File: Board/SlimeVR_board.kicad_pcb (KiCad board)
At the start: 2 copper layers, 61 x 50 mm, 46 parts, among them IC1 HT7833, J1 USB_C_Receptacle_USB2.0_16P, J2 JST-PH, J3 SMD_Pads, J4 SMD_Pads, J5 Conn_01x01_Pin, J6 Conn_01x01_Pin, J7 JTX-HX-A-1, J8 JTX-HX-A-1, Q1 DMP3099L-7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

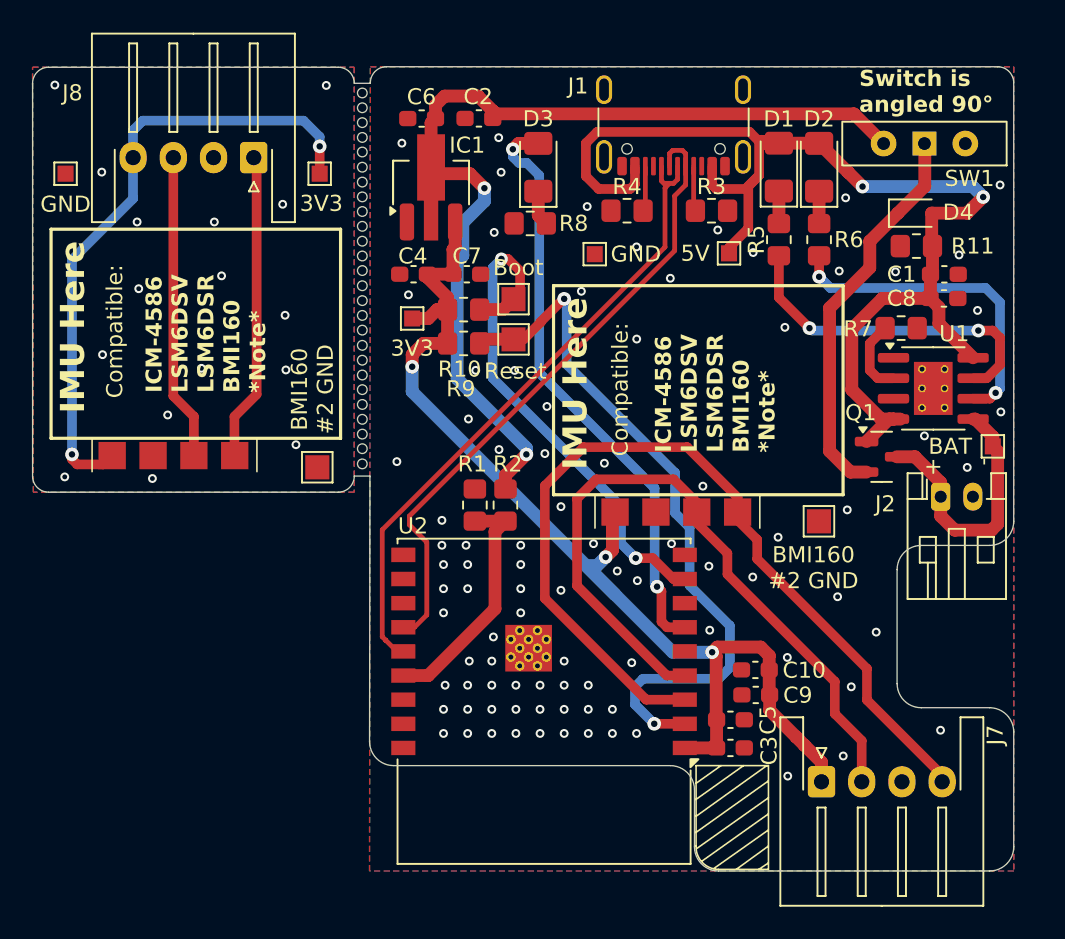
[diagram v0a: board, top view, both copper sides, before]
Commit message: Nweset Board update
Update log:
- Moved 3.3 conventor closer to esp for more stability
- Properly labeled Boot and Reset pads with own GND
- New and remade grafic
- Two capacitators no more needed (material saving :D)
- New Logo (I got some logo of my probebly will change idk)
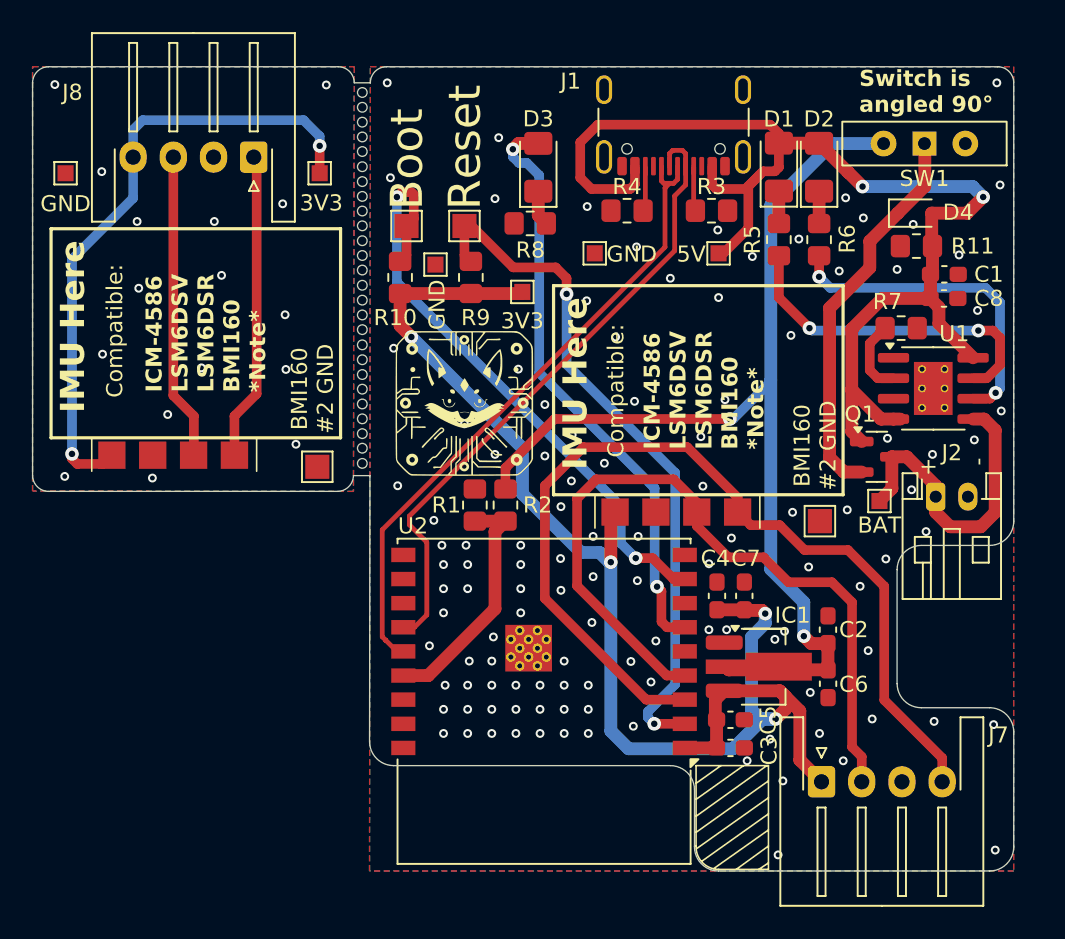
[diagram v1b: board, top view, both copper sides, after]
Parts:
- removed C10: 100nF, Capacitor_SMD:C_0603_1608Metric_Pad1.08x0.95mm_HandSolder
- removed C9: 1uF, Capacitor_SMD:C_0603_1608Metric_Pad1.08x0.95mm_HandSolder
- removed the GND at (37.6, 26.4)
- added GND: TestPoint_Pad_1.0x1.0mm, TestPoint:TestPoint_Pad_1.0x1.0mm, F.Cu at (60.6, 32.0)
- added GND: TestPoint_Pad_1.0x1.0mm, TestPoint:TestPoint_Pad_1.0x1.0mm, F.Cu at (37.6, 26.3)
- moved C6 43.3 mm to (85.0, 58.1), turned to -90 degrees
- moved C2 38.5 mm to (85.0, 54.7), turned to 90 degrees
- moved IC1 36.5 mm to (81.0, 57.0), turned to 0 degrees
- moved C4 27.5 mm to (78.1, 52.6), turned to 90 degrees
- moved C7 26.4 mm to (79.8, 52.6), turned to 90 degrees
- moved J6 8.06 mm to (58.8, 29.6)
- moved BAT 7.83 mm to (88.2, 46.7)
- moved J5 7.68 mm to (62.4, 29.6)
- moved 3V3 7.05 mm to (66.0, 33.7)
- moved R10 4.43 mm to (58.4, 32.8), turned to 90 degrees
- moved R9 4.12 mm to (62.8, 32.8), turned to 90 degrees
- moved 5V 0.65 mm to (78.2, 31.3)
- moved J2 0.31 mm to (91.7, 46.4)
- moved Q1 0.30 mm to (88.0, 44.0)
- moved BMI160 #2 GND 0.06 mm to (84.5, 48.0)
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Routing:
- net +3.3V: track 109.9 -> 124.9 mm, vias 5 -> 6
- net Net-(J6-Pin_1): track 31.9 -> 37.9 mm
- net +5V: track 75.6 -> 79.7 mm
- net SCL: track 63.6 -> 66.5 mm
- net SDA: track 74.7 -> 77.3 mm
- net +BATT: track 16.8 -> 19.4 mm
- net Net-(J5-Pin_1): track 45.1 -> 43.3 mm
- net Net-(SW1-C): track 65.1 -> 66.1 mm
- net Earth: vias 106 -> 132
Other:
- outline, holes or cut-outs redrawn
- board text added: "Ver.: 3W"
- board text removed: "Ver.: 2.6W"
